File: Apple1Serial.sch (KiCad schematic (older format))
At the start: 35 parts, among them U7402 7402

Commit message: Fixed element values on schematics
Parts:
- 74S257mux1, 74S257mux2, 8T97buf1, 8T97buf2: footprint Package_DIP:DIP-16_W7.62mm_Socket_LongPads -> Package_DIP:DIP-16_W7.62mm_LongPads
- AT28C64B1: value AT28C64B -> 28C64; footprint Package_DIP:DIP-28_W15.24mm_Socket_LongPads -> Package_DIP:DIP-28_W15.24mm_LongPads
- ATmega328P1: value ATmega328P-PU -> ATmega328P; footprint Package_DIP:DIP-28_W7.62mm_Socket_LongPads -> Package_DIP:DIP-28_W7.62mm_LongPads
- GAL20V8B1: value GAL20V8B -> GAL20V8; footprint Package_DIP:DIP-24_W7.62mm_Socket_LongPads -> Package_DIP:DIP-24_W7.62mm_LongPads
- LED1: footprint Package_DIP:DIP-8_W7.62mm_Socket_LongPads -> Package_DIP:DIP-8_W7.62mm_LongPads
- RX_LED1: value LED -> RX
- TX_LED1: value LED -> TX
- U7402: footprint Package_DIP:DIP-14_W7.62mm_Socket_LongPads -> Package_DIP:DIP-14_W7.62mm_LongPads
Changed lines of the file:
@@
 P 2950 1950
 F 0 "AT28C64B1" H 3500 2215 50  0000 C CNN
-F 1 "AT28C64B" H 3500 2124 50  0001 C CNN
-F 2 "Package_DIP:DIP-28_W15.24mm_Socket_LongPads" H 3900 2050 50  0001 L CNN
+F 1 "28C64" H 3500 2124 50  0001 C CNN
+F 2 "Package_DIP:DIP-28_W15.24mm_LongPads" H 3900 2050 50  0001 L CNN
 F 3 "http://www.atmel.com/images/doc0270.pdf" H 3900 1950 50  0001 L CNN
 F 4 "AT28C64B-15PU, Parallel EEPROM Memory 64kbit, Parallel, 150ns 4.5  5.5 V, 28-Pin PDIP" H 3900 1850 50  0001 L CNN "Description"
@@
 P 3100 5050
 F 0 "GAL20V8B1" H 3650 5315 50  0000 C CNN
-F 1 "GAL20V8B" H 3650 5224 50  0001 C CNN
-F 2 "Package_DIP:DIP-24_W7.62mm_Socket_LongPads" H 4050 5150 50  0001 L CNN
+F 1 "GAL20V8" H 3650 5224 50  0001 C CNN
+F 2 "Package_DIP:DIP-24_W7.62mm_LongPads" H 4050 5150 50  0001 L CNN
 F 3 "http://uk.rs-online.com/web/p/products/4142962" H 4050 5050 50  0001 L CNN
 F 4 "Lattice Semiconductor GAL20V8B-15LP, SPLD GAL, GAL20V8B 8 Macro Cells, 8 I/O, 62.5MHz External 15ns EECMOS 24-Pin PDIP" H 4050 4950 50  0001 L CNN "Description"
@@
 F 0 "U7402" H 4300 4575 50  0001 C CNN
 F 1 "7402" H 4300 4484 50  0000 C CNN
-F 2 "Package_DIP:DIP-14_W7.62mm_Socket_LongPads" H 4300 4250 50  0001 C CNN
+F 2 "Package_DIP:DIP-14_W7.62mm_LongPads" H 4300 4250 50  0001 C CNN
 F 3 "http://www.ti.com/lit/gpn/sn7402" H 4300 4250 50  0001 C CNN
 	1    4300 4250
@@
 F 0 "U7402" H 6350 4175 50  0001 C CNN
 F 1 "7402" H 6350 4084 50  0000 C CNN
-F 2 "Package_DIP:DIP-14_W7.62mm_Socket_LongPads" H 6350 3850 50  0001 C CNN
+F 2 "Package_DIP:DIP-14_W7.62mm_LongPads" H 6350 3850 50  0001 C CNN
 F 3 "http://www.ti.com/lit/gpn/sn7402" H 6350 3850 50  0001 C CNN
 	2    6350 3850
@@
 F 0 "U7402" H 3600 7725 50  0001 C CNN
 F 1 "7402" H 3600 7634 50  0000 C CNN
-F 2 "Package_DIP:DIP-14_W7.62mm_Socket_LongPads" H 3600 7400 50  0001 C CNN
+F 2 "Package_DIP:DIP-14_W7.62mm_LongPads" H 3600 7400 50  0001 C CNN
 F 3 "http://www.ti.com/lit/gpn/sn7402" H 3600 7400 50  0001 C CNN
 	3    3600 7400
@@
 F 0 "U7402" H 4600 7825 50  0001 C CNN
 F 1 "7402" H 4600 7734 50  0000 C CNN
-F 2 "Package_DIP:DIP-14_W7.62mm_Socket_LongPads" H 4600 7500 50  0001 C CNN
+F 2 "Package_DIP:DIP-14_W7.62mm_LongPads" H 4600 7500 50  0001 C CNN
 F 3 "http://www.ti.com/lit/gpn/sn7402" H 4600 7500 50  0001 C CNN
 	4    4600 7500
@@
 F 0 "U7402" H 7530 5796 50  0000 L CNN
 F 1 "7402" H 7530 5705 50  0000 L CNN
-F 2 "Package_DIP:DIP-14_W7.62mm_Socket_LongPads" H 7300 5750 50  0001 C CNN
+F 2 "Package_DIP:DIP-14_W7.62mm_LongPads" H 7300 5750 50  0001 C CNN
 F 3 "http://www.ti.com/lit/gpn/sn7402" H 7300 5750 50  0001 C CNN
 	5    7300 5750
@@
 F 0 "74S257mux2" H 5700 6439 50  0000 C CNN
 F 1 "74S257" H 5700 6440 50  0001 C CNN
-F 2 "Package_DIP:DIP-16_W7.62mm_Socket_LongPads" H 5700 5450 50  0001 C CNN
+F 2 "Package_DIP:DIP-16_W7.62mm_LongPads" H 5700 5450 50  0001 C CNN
 F 3 "http://www.ti.com/lit/gpn/sn74LS257" H 5700 5450 50  0001 C CNN
 	1    5700 5450
@@
 F 0 "74S257mux1" H 5700 3631 50  0000 C CNN
 F 1 "74S257" H 5700 3540 50  0001 C CNN
-F 2 "Package_DIP:DIP-16_W7.62mm_Socket_LongPads" H 5700 2550 50  0001 C CNN
+F 2 "Package_DIP:DIP-16_W7.62mm_LongPads" H 5700 2550 50  0001 C CNN
 F 3 "http://www.ti.com/lit/gpn/sn74LS257" H 5700 2550 50  0001 C CNN
 	1    5700 2550
@@
 F 0 "8T97buf1" H 7500 2531 50  0000 C CNN
 F 1 "8T97" H 7500 2440 50  0001 C CNN
-F 2 "Package_DIP:DIP-16_W7.62mm_Socket_LongPads" H 7500 1650 50  0001 C CNN
+F 2 "Package_DIP:DIP-16_W7.62mm_LongPads" H 7500 1650 50  0001 C CNN
 F 3 "http://www.ti.com/lit/gpn/sn74LS367" H 7500 1650 50  0001 C CNN
 	1    7500 1650
@@
 F 0 "8T97buf2" H 7500 4631 50  0000 C CNN
 F 1 "8T97" H 7500 4540 50  0001 C CNN
-F 2 "Package_DIP:DIP-16_W7.62mm_Socket_LongPads" H 7500 3750 50  0001 C CNN
+F 2 "Package_DIP:DIP-16_W7.62mm_LongPads" H 7500 3750 50  0001 C CNN
 F 3 "http://www.ti.com/lit/gpn/sn74LS367" H 7500 3750 50  0001 C CNN
 	1    7500 3750
@@
 P 9600 3150
 F 0 "ATmega328P1" H 8956 3196 50  0000 R CNN
-F 1 "ATmega328P-PU" H 8956 3105 50  0001 R CNN
-F 2 "Package_DIP:DIP-28_W7.62mm_Socket_LongPads" H 9600 3150 50  0001 C CIN
+F 1 "ATmega328P" H 8956 3105 50  0001 R CNN
+F 2 "Package_DIP:DIP-28_W7.62mm_LongPads" H 9600 3150 50  0001 C CIN
 F 3 "http://ww1.microchip.com/downloads/en/DeviceDoc/ATmega328_P%20AVR%20MCU%20with%20picoPower%20Technology%20Data%20Sheet%2040001984A.pdf" H 9600 3150 50  0001 C CNN
 	1    9600 3150
@@
 F 0 "LED1" H 9050 5567 50  0000 C CNN
 F 1 "LM358" H 9050 5476 50  0000 C CNN
-F 2 "Package_DIP:DIP-8_W7.62mm_Socket_LongPads" H 9050 5200 50  0001 C CNN
+F 2 "Package_DIP:DIP-8_W7.62mm_LongPads" H 9050 5200 50  0001 C CNN
 F 3 "http://www.ti.com/lit/ds/symlink/lm2904-n.pdf" H 9050 5200 50  0001 C CNN
 	1    9050 5200
@@
 F 0 "LED1" H 9050 6267 50  0000 C CNN
 F 1 "LM358" H 9050 6176 50  0000 C CNN
-F 2 "Package_DIP:DIP-8_W7.62mm_Socket_LongPads" H 9050 5900 50  0001 C CNN
+F 2 "Package_DIP:DIP-8_W7.62mm_LongPads" H 9050 5900 50  0001 C CNN
 F 3 "http://www.ti.com/lit/ds/symlink/lm2904-n.pdf" H 9050 5900 50  0001 C CNN
 	2    9050 5900
@@
 F 0 "LED1" H 8008 5646 50  0000 L CNN
 F 1 "LM358" H 8008 5555 50  0000 L CNN
-F 2 "Package_DIP:DIP-8_W7.62mm_Socket_LongPads" H 8050 5600 50  0001 C CNN
+F 2 "Package_DIP:DIP-8_W7.62mm_LongPads" H 8050 5600 50  0001 C CNN
 F 3 "http://www.ti.com/lit/ds/symlink/lm2904-n.pdf" H 8050 5600 50  0001 C CNN
 	3    8050 5600
@@
 P 10050 5900
 F 0 "RX_LED1" H 10043 6116 50  0000 C CNN
-F 1 "LED" H 10043 6025 50  0000 C CNN
+F 1 "RX" H 10043 6025 50  0000 C CNN
 F 2 "LED_THT:LED_D3.0mm" H 10050 5900 50  0001 C CNN
 F 3 "~" H 10050 5900 50  0001 C CNN
@@
 P 10050 5200
 F 0 "TX_LED1" H 10043 5416 50  0000 C CNN
-F 1 "LED" H 10043 5325 50  0000 C CNN
+F 1 "TX" H 10043 5325 50  0000 C CNN
 F 2 "LED_THT:LED_D3.0mm" H 10050 5200 50  0001 C CNN
 F 3 "~" H 10050 5200 50  0001 C CNN

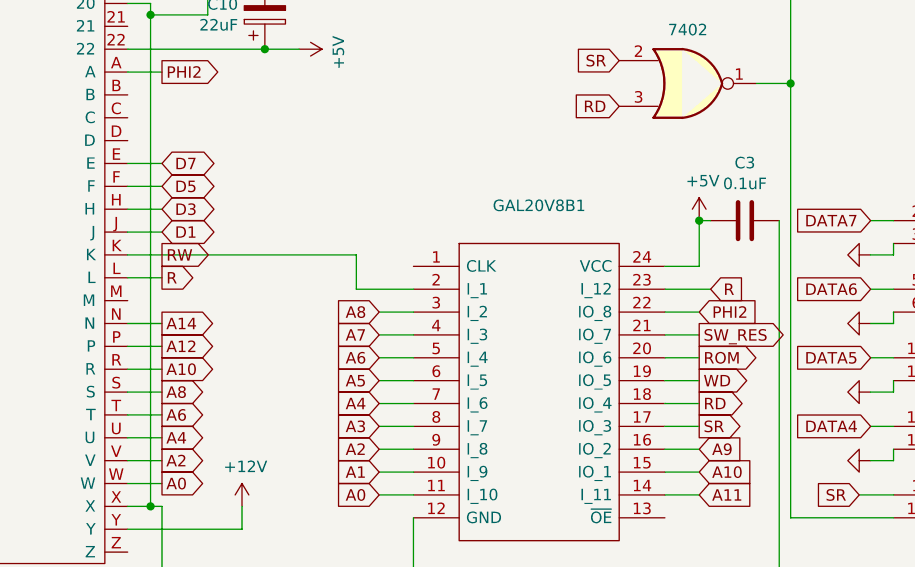
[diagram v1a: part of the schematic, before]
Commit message: replaced R with T
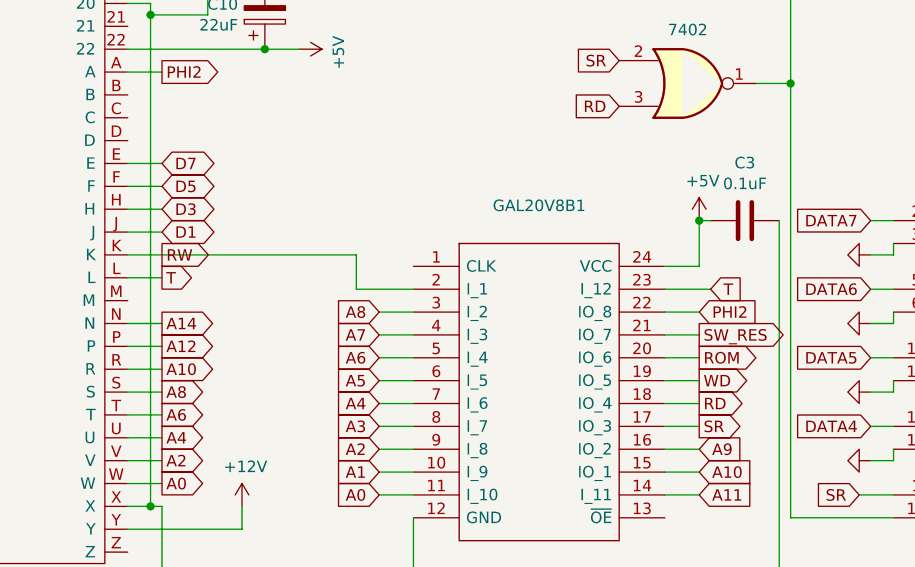
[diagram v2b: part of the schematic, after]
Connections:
- net R renamed T
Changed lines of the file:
@@
 	4350 5050 4200 5050
 Text GLabel 2000 5100 2    50   Output ~ 0
-R
+T
 Wire Wire Line
 	1850 5100 2000 5100
 Text GLabel 4400 5150 2    50   Input ~ 0
-R
+T
 Wire Wire Line
 	4200 5150 4400 5150

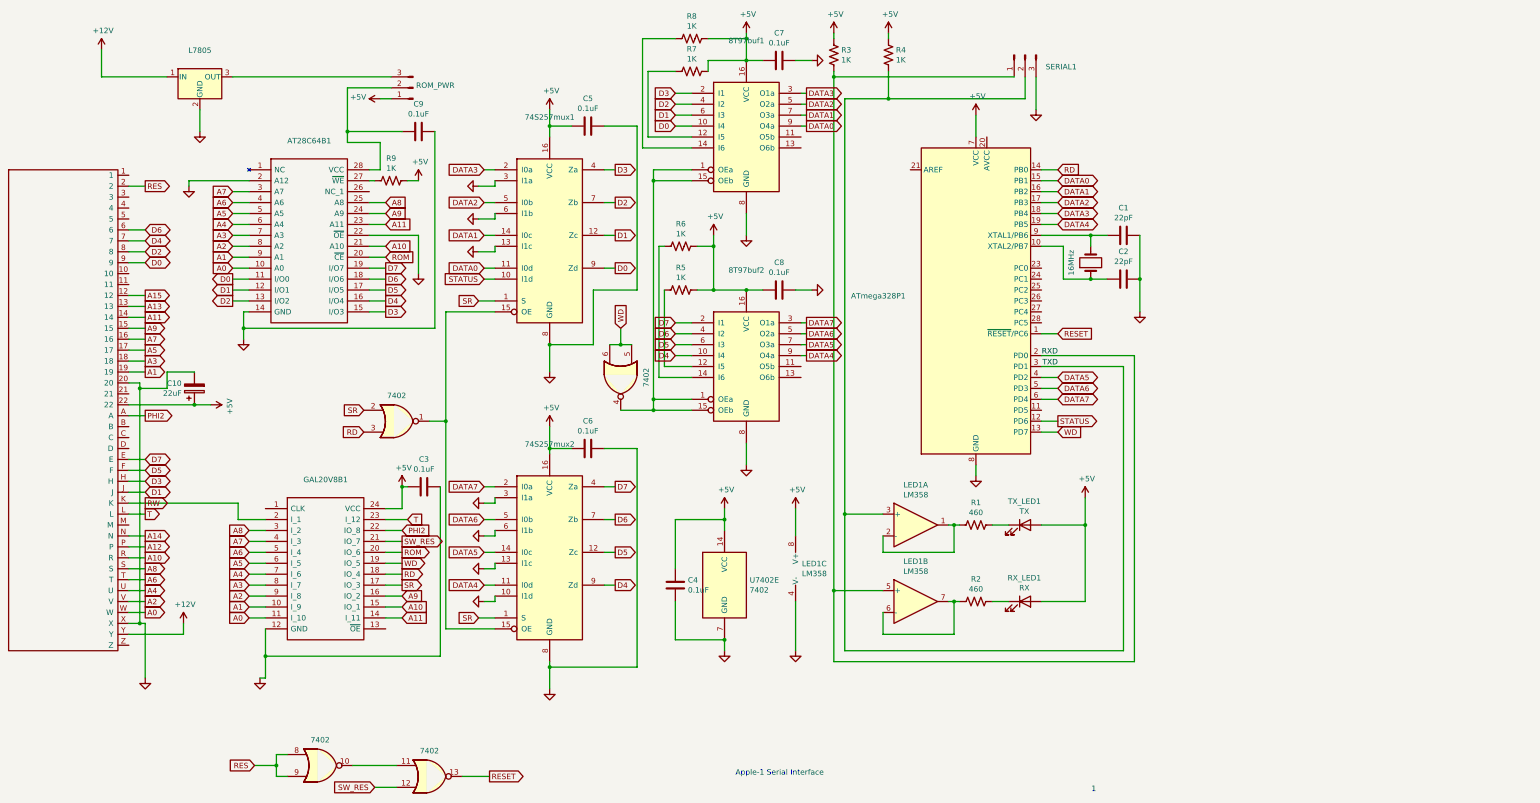
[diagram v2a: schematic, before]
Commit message: Added DB9 rs232 connector
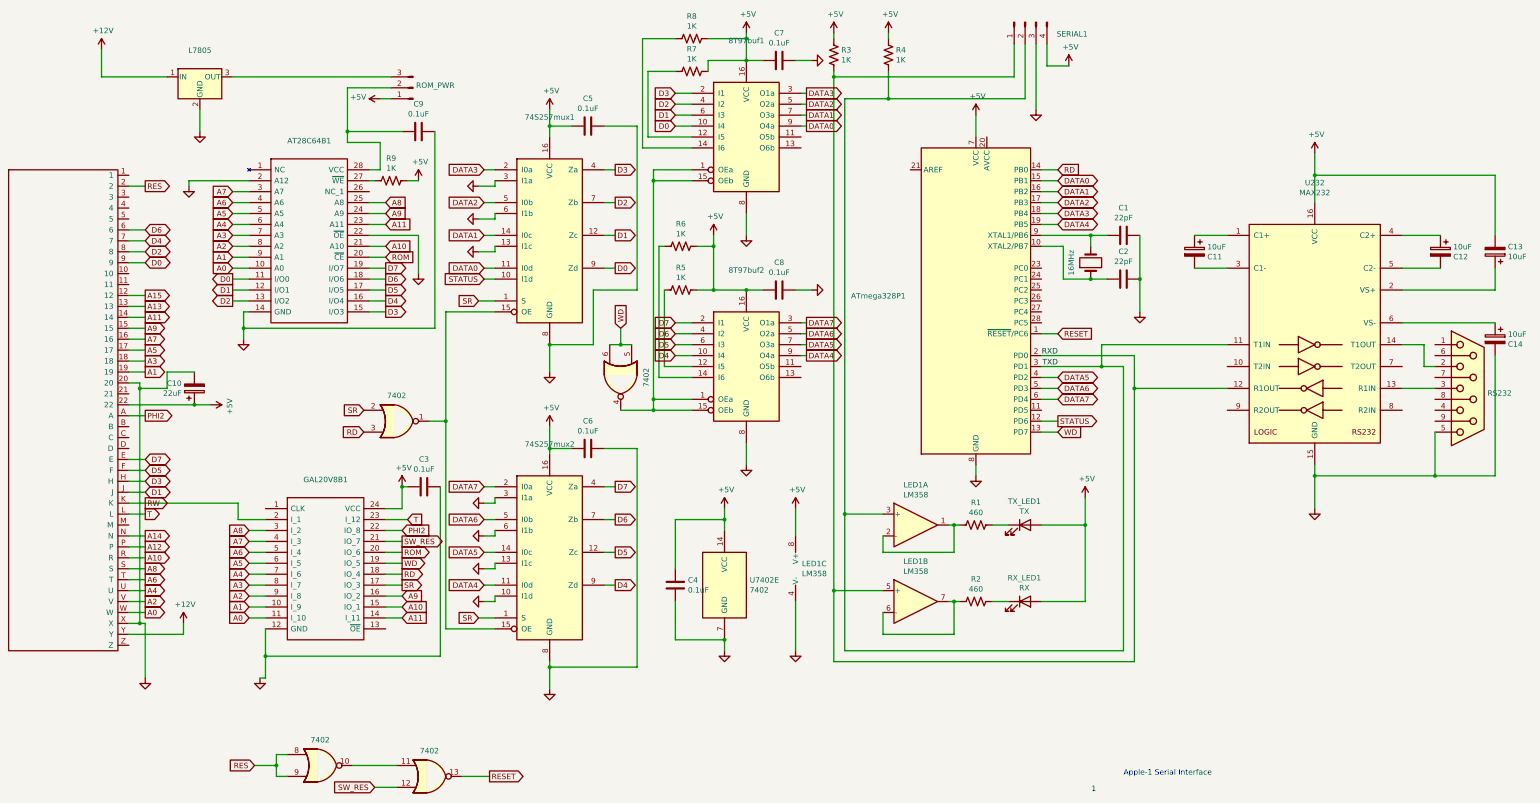
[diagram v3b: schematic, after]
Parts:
- removed SERIAL1: SERIAL, Connector_PinHeader_2.54mm:PinHeader_1x03_P2.54mm_Vertical, symbol Connector:Conn_01x03_Male
- added C11, C12, C13, C14: 10uF, Capacitor_THT:CP_Radial_D4.0mm_P2.00mm, symbol Device:CP
- added RS232: DB9_Female_MountingHoles, Connector_Dsub:DSUB-9_Female_Horizontal_P2.77x2.84mm_EdgePinOffset4.94mm_Housed_MountingHolesOffset7.48mm, symbol Connector:DB9_Female
- added SERIAL1: SERIAL1, Connector_PinHeader_2.54mm:PinHeader_1x04_P2.54mm_Vertical, symbol Connector:Conn_01x04_Male
- added U232: MAX232, Package_DIP:DIP-16_W7.62mm_LongPads, symbol Interface_UART:MAX232
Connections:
- net +5V: now also C13.2, SERIAL1.4 (Pin_4), U232.16 (VCC)
- net GND: now also C14.2, RS232.5, SERIAL1.3 (Pin_3), U232.15 (GND)
- net RXD: now also SERIAL1.1 (Pin_1), U232.12 (R1OUT)
- net TXD: now also SERIAL1.2 (Pin_2), U232.11 (T1IN)
- new net: C11.1, U232.1 (C1+)
- new net: RS232.3, U232.13 (R1IN)
- new net: RS232.2, U232.14 (T1OUT)
- new net: C13.1, U232.2 (VS+)
- new net: C11.2, U232.3 (C1-)
- new net: C12.1, U232.4 (C2+)
- new net: C12.2, U232.5 (C2-)
- new net: C14.1, U232.6 (VS-)
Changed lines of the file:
@@
 EELAYER 30 0
 EELAYER END
-$Descr A4 11693 8268
+$Descr User 15236 8268
 encoding utf-8
 Sheet 1 1
@@
 	1    0    0    -1
 $EndComp
-Text Notes 7400 7500 0    50   ~ 0
+Text Notes 10950 7500 0    50   ~ 0
 Apple-1 Serial Interface
 $Comp
@@
 Connection ~ 10600 5200
 $Comp
-L Connector:Conn_01x03_Male SERIAL1
-U 1 1 5F0216A9
-P 10050 900
-F 0 "SERIAL1" V 10158 712 50  0000 R CNN
-F 1 "SERIAL" V 10113 712 50  0001 R CNN
-F 2 "Connector_PinHeader_2.54mm:PinHeader_1x03_P2.54mm_Vertical" H 10050 900 50  0001 C CNN
-F 3 "~" H 10050 900 50  0001 C CNN
-	1    10050 900
-	0    -1   1    0
-$EndComp
-$Comp
 L power:GND #PWR0118
 U 1 1 5F0268E3
@@
 	1    0    0    -1
 $EndComp
-Wire Wire Line
-	10150 1100 10150 1400
 Wire Wire Line
 	9400 5200 9400 5450
@@
 Connection ~ 10650 2950
 Wire Wire Line
-	11050 3650 11050 6450
+	11050 3650 11050 3950
 Wire Wire Line
 	11050 6450 8300 6450
 Wire Wire Line
-	10200 3750 10950 3750
-Wire Wire Line
-	10950 3750 10950 6350
+	10200 3750 10750 3750
 Wire Wire Line
 	10950 6350 8400 6350
@@
 $EndComp
 Wire Wire Line
-	9950 1100 8300 1100
-Wire Wire Line
-	10050 1100 10050 1300
-Wire Wire Line
 	10050 1300 8800 1300
 $Comp
@@
 	1    0    0    -1
 $EndComp
-Wire Wire Line
-	8300 1050 8300 1100
-Connection ~ 8300 1100
 Wire Wire Line
 	8800 1050 8800 1300
@@
 	5100 2950 5200 2950
 Wire Wire Line
-	8300 1100 8300 5800
-Wire Wire Line
 	8400 1300 8400 5100
 Wire Wire Line
@@
 Wire Wire Line
 	4400 2050 4500 2050
+$Comp
+L Connector:Conn_01x04_Male SERIAL1
+U 1 1 63C7BCB6
+P 10050 600
+F 0 "SERIAL1" V 10158 312 50  0000 R CNN
+F 1 "SERIAL1" H 10158 790 50  0001 C CNN
+F 2 "Connector_PinHeader_2.54mm:PinHeader_1x04_P2.54mm_Vertical" H 10050 600 50  0001 C CNN
+F 3 "~" H 10050 600 50  0001 C CNN
+	1    10050 600
+	0    -1   1    0
+$EndComp
+Wire Wire Line
+	8300 1100 8300 5800
+Wire Wire Line
+	8300 1050 8300 1100
+Connection ~ 8300 1100
+Wire Wire Line
+	9950 1100 8300 1100
+Wire Wire Line
+	9950 1100 9950 800
+Wire Wire Line
+	10050 800  10050 1300
+Wire Wire Line
+	10150 800  10150 1400
+$Comp
+L power:+5V #PWR0141
+U 1 1 63D2431A
+P 10450 1000
+F 0 "#PWR0141" H 10450 850 50  0001 C CNN
+F 1 "+5V" H 10465 1173 50  0000 C CNN
+F 2 "" H 10450 1000 50  0001 C CNN
+F 3 "" H 10450 1000 50  0001 C CNN
+	1    10450 1000
+	1    0    0    -1
+$EndComp
+Wire Wire Line
+	10450 1000 10250 1000
+Wire Wire Line
+	10250 1000 10250 800
+$Comp
+L Interface_UART:MAX232 U232
+U 1 1 645D7665
+P 12700 3450
+F 0 "U232" H 12700 4831 50  0000 C CNN
+F 1 "MAX232" H 12700 4740 50  0000 C CNN
+F 2 "Package_DIP:DIP-16_W7.62mm_LongPads" H 12750 2400 50  0001 L CNN
+F 3 "http://www.ti.com/lit/ds/symlink/max232.pdf" H 12700 3550 50  0001 C CNN
+	1    12700 3450
+	1    0    0    -1
+$EndComp
+$Comp
+L power:+5V #PWR0142
+U 1 1 64619BD0
+P 12700 1800
+F 0 "#PWR0142" H 12700 1650 50  0001 C CNN
+F 1 "+5V" H 12715 1973 50  0000 C CNN
+F 2 "" H 12700 1800 50  0001 C CNN
+F 3 "" H 12700 1800 50  0001 C CNN
+	1    12700 1800
+	1    0    0    -1
+$EndComp
+$Comp
+L power:GND #PWR0143
+U 1 1 6461B51C
+P 12700 5050
+F 0 "#PWR0143" H 12700 4800 50  0001 C CNN
+F 1 "GND" H 12705 4877 50  0001 C CNN
+F 2 "" H 12700 5050 50  0001 C CNN
+F 3 "" H 12700 5050 50  0001 C CNN
+	1    12700 5050
+	1    0    0    -1
+$EndComp
+Wire Wire Line
+	12700 1800 12700 2000
+Wire Wire Line
+	12700 4650 12700 4750
+$Comp
+L Device:CP C12
+U 1 1 64655A9C
+P 13850 2700
+F 0 "C12" H 13733 2654 50  0000 R CNN
+F 1 "10uF" H 13733 2745 50  0000 R CNN
+F 2 "Capacitor_THT:CP_Radial_D4.0mm_P2.00mm" H 13888 2550 50  0001 C CNN
+F 3 "~" H 13850 2700 50  0001 C CNN
+	1    13850 2700
+	-1   0    0    -1
+$EndComp
+Wire Wire Line
+	13500 2550 13850 2550
+Wire Wire Line
+	13500 2850 13850 2850
+$Comp
+L Device:CP C11
+U 1 1 64703922
+P 11600 2700
+F 0 "C11" H 11483 2654 50  0000 R CNN
+F 1 "10uF" H 11483 2745 50  0000 R CNN
+F 2 "Capacitor_THT:CP_Radial_D4.0mm_P2.00mm" H 11638 2550 50  0001 C CNN
+F 3 "~" H 11600 2700 50  0001 C CNN
+	1    11600 2700
+	-1   0    0    -1
+$EndComp
+Wire Wire Line
+	11600 2550 11900 2550
+Wire Wire Line
+	11600 2850 11900 2850
+$Comp
+L Connector:DB9_Female RS232
+U 1 1 64741FCD
+P 14100 3950
+F 0 "RS232" H 14280 3906 50  0000 L CNN
+F 1 "DB9_Female_MountingHoles" H 14280 3861 50  0001 L CNN
+F 2 "Connector_Dsub:DSUB-9_Female_Horizontal_P2.77x2.84mm_EdgePinOffset4.94mm_Housed_MountingHolesOffset7.48mm" H 14100 3950 50  0001 C CNN
+F 3 " ~" H 14100 3950 50  0001 C CNN
+	1    14100 3950
+	1    0    0    -1
+$EndComp
+Wire Wire Line
+	10950 3750 10950 6350
+Connection ~ 10750 3750
+Wire Wire Line
+	10750 3750 10950 3750
+Wire Wire Line
+	10750 3750 10750 3550
+Wire Wire Line
+	10750 3550 11900 3550
+Connection ~ 11050 3950
+Wire Wire Line
+	11050 3950 11050 6450
+Wire Wire Line
+	11050 3950 11900 3950
+$Comp
+L Device:CP C13
+U 1 1 647BC16E
+P 14350 2700
+F 0 "C13" H 14233 2654 50  0000 R CNN
+F 1 "10uF" H 14233 2745 50  0000 R CNN
+F 2 "Capacitor_THT:CP_Radial_D4.0mm_P2.00mm" H 14388 2550 50  0001 C CNN
+F 3 "~" H 14350 2700 50  0001 C CNN
+	1    14350 2700
+	-1   0    0    1
+$EndComp
+Wire Wire Line
+	14350 2850 14350 3050
+Wire Wire Line
+	14350 3050 13500 3050
+Wire Wire Line
+	14350 2550 14350 2000
+Wire Wire Line
+	14350 2000 12700 2000
+Connection ~ 12700 2000
+Wire Wire Line
+	12700 2000 12700 2250
+$Comp
+L Device:CP C14
+U 1 1 64813BF4
+P 14350 3500
+F 0 "C14" H 14233 3454 50  0000 R CNN
+F 1 "10uF" H 14233 3545 50  0000 R CNN
+F 2 "Capacitor_THT:CP_Radial_D4.0mm_P2.00mm" H 14388 3350 50  0001 C CNN
+F 3 "~" H 14350 3500 50  0001 C CNN
+	1    14350 3500
+	-1   0    0    -1
+$EndComp
+Wire Wire Line
+	14350 3350 13500 3350
+Wire Wire Line
+	14350 3650 14350 4750
+Wire Wire Line
+	14350 4750 13800 4750
+Connection ~ 12700 4750
+Wire Wire Line
+	12700 4750 12700 5050
+Wire Wire Line
+	13500 3550 13700 3550
+Wire Wire Line
+	13700 3550 13700 3750
+Wire Wire Line
+	13700 3750 13800 3750
+Wire Wire Line
+	13500 3950 13800 3950
+Wire Wire Line
+	13800 4350 13800 4750
+Connection ~ 13800 4750
+Wire Wire Line
+	13800 4750 12700 4750
 $EndSCHEMATC
